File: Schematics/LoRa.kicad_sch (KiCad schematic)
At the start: 2 parts, among them J7 Conn_Coaxial_Small, U5 RFM95W-915S2

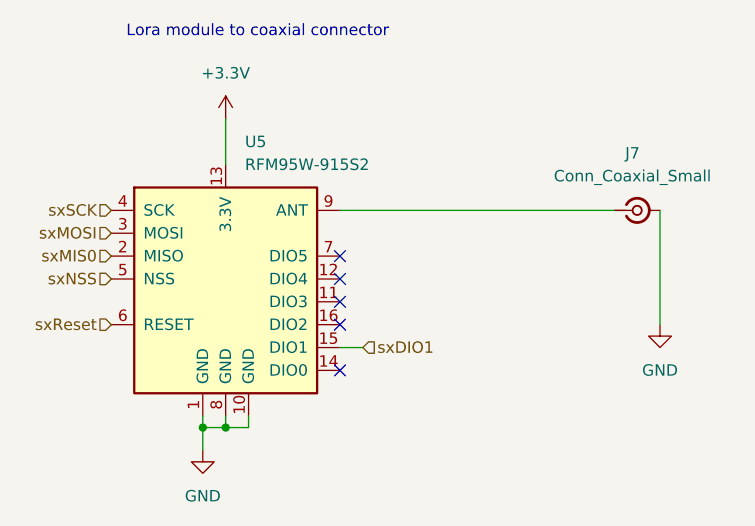
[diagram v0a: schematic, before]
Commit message: added DIO0 and DIO2 pins to read lora module outputs
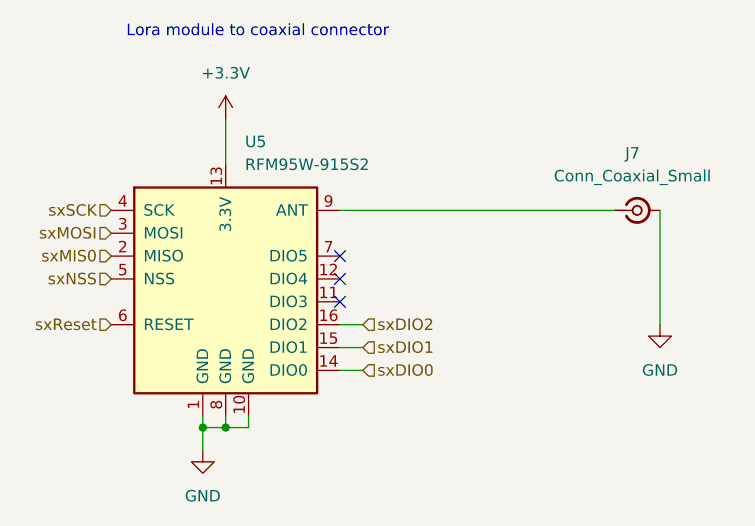
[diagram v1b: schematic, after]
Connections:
- net sxDIO0: now reaches U5.14 (DIO0)
- net sxDIO2: now reaches U5.16 (DIO2)
- no-connect marks 5 -> 3
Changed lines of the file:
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@@
-	)
-	(no_connect
-		(at 143.51 88.9)
 	)
 	(no_connect
@@
 		(at 143.51 81.28)
 	)
-	(no_connect
-		(at 143.51 93.98)
+	(wire
+		(pts
+			(xy 130.81 100.33) (xy 128.27 100.33)
+		)
+		(stroke
+			(width 0)
+			(type default)
+		)
 	)
 	(wire
 		(pts
-			(xy 130.81 100.33) (xy 128.27 100.33)
+			(xy 146.05 88.9) (xy 143.51 88.9)
+		)
+		(stroke
+			(width 0)
+			(type default)
+		)
+	)
+	(wire
+		(pts
+			(xy 146.05 93.98) (xy 143.51 93.98)
 		)
 		(stroke
@@
 		)
 	)
+	(hierarchical_label "sxDIO0"
+		(shape input)
+		(at 146.05 93.98 0)
+		(effects
+			(font
+				(size 1.27 1.27)
+			)
+			(justify left)
+		)
+	)
 	(hierarchical_label "sxDIO1"
 		(shape input)
@@
 		)
 	)
+	(hierarchical_label "sxDIO2"
+		(shape input)
+		(at 146.05 88.9 0)
+		(effects
+			(font
+				(size 1.27 1.27)
+			)
+			(justify left)
+		)
+	)
